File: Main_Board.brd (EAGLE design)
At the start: 160 x 100 mm, 73 parts, among them U1 RN4020RN4020, U2 LMS8117, U3 5V_BUCK_REG, Y1 MC-30632.768K-E3, Y2 MA-5066-25.0000M-C0

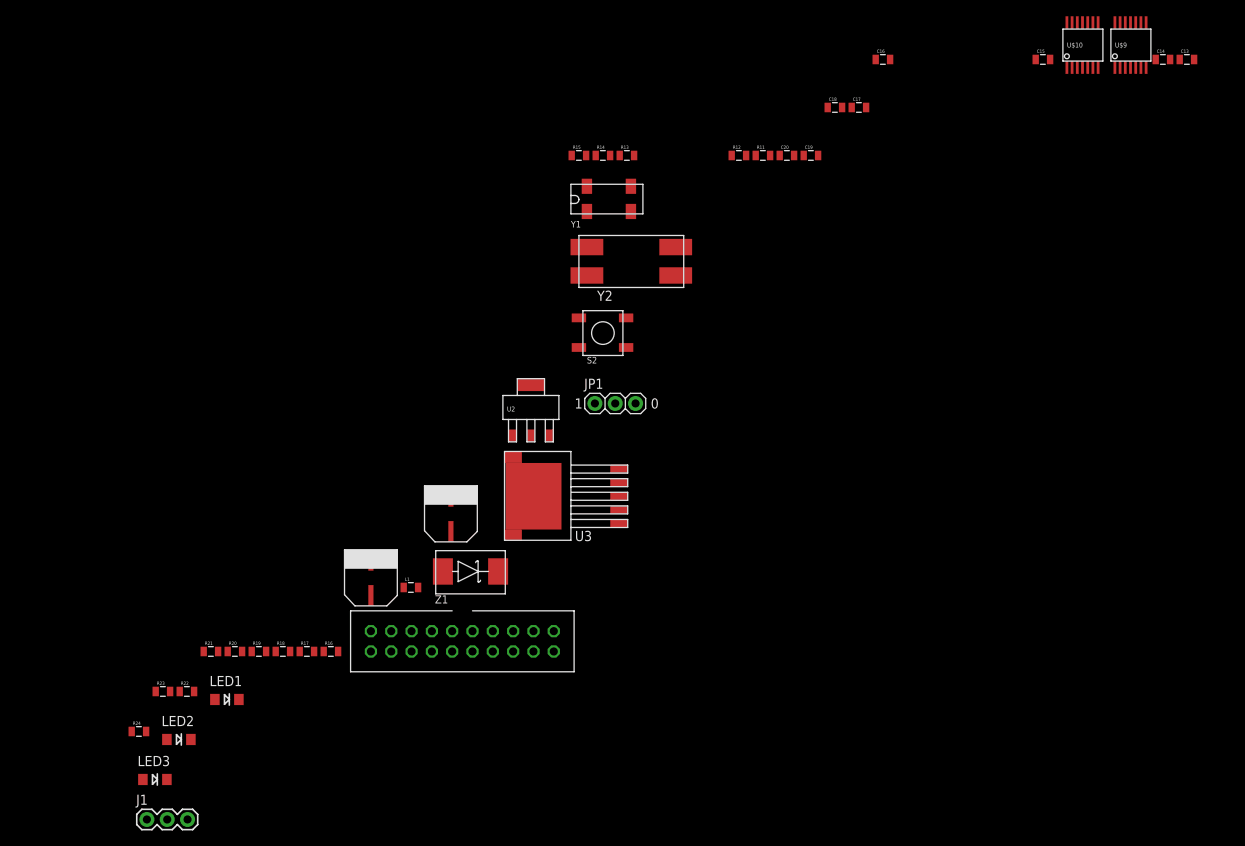
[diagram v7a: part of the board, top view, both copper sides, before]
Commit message: Added cap values
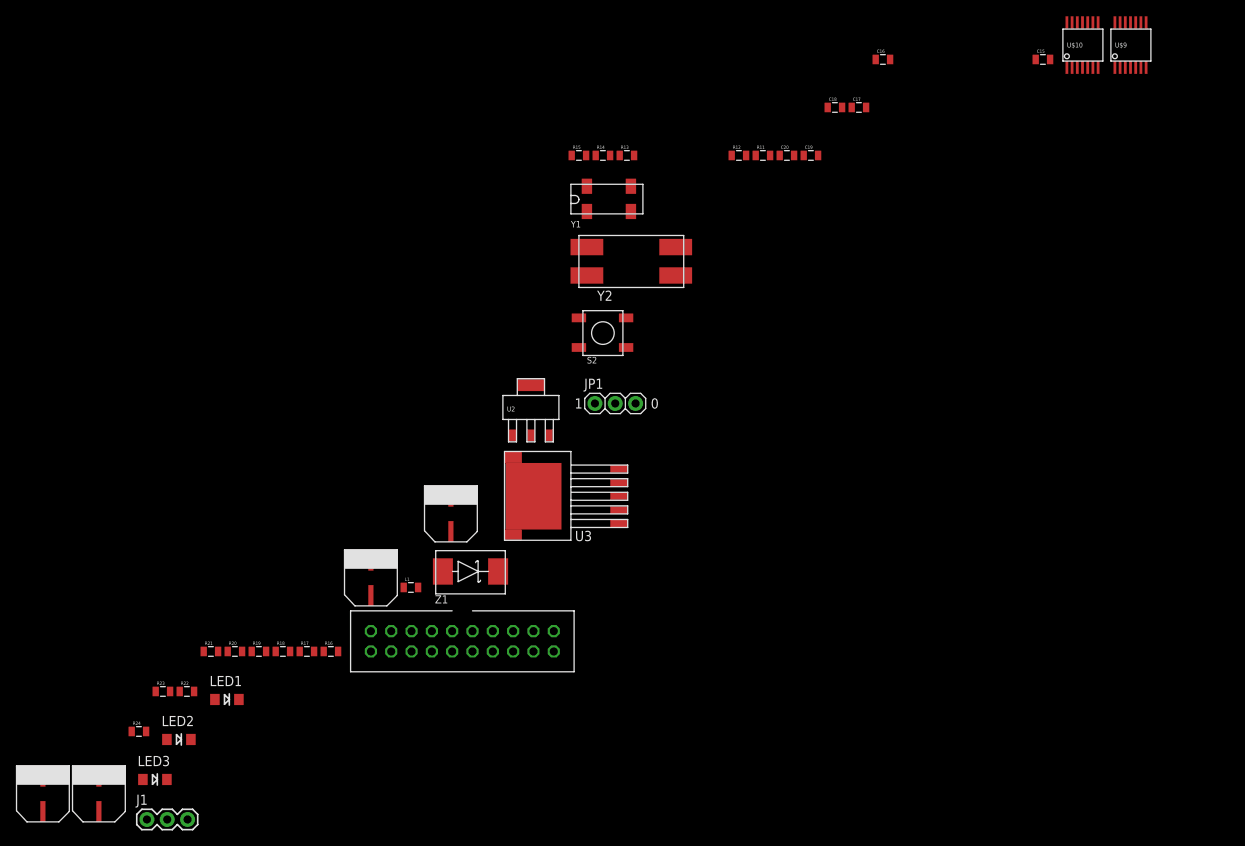
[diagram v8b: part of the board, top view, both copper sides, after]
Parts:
- removed C13, C14: (no value), SparkFun-Capacitors:0805
- added U$13, U$14: 10uF, BB8:RADIAL_CAN_SMD
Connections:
- net 3.3V: now also U$14.P$1; no longer C14.1
- net 5V: now also U$13.P$1; no longer C13.1
- net GND: now also U$13.P$2, U$14.P$2; no longer C13.2, C14.2
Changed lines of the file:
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@@
 <element name="FRAME1" library="SparkFun-Aesthetics" package="CREATIVE_COMMONS" value="FRAME-LEDGER" x="-87" y="-123"/>
 <element name="FRAME3" library="SparkFun-Aesthetics" package="CREATIVE_COMMONS" value="FRAME-LEDGER" x="-87" y="-132"/>
-<element name="C13" library="SparkFun-Capacitors" package="0805" value="" x="-118" y="-131"/>
-<element name="C14" library="SparkFun-Capacitors" package="0805" value="" x="-121" y="-131"/>
 <element name="U$9" library="BB8" package="14-TSSOP" value="SN74LV4T125" x="-127" y="-132"/>
 <element name="U$10" library="BB8" package="14-TSSOP" value="SN74LV4T125" x="-133" y="-132"/>
@@
 <element name="LED3" library="LilyPad-Wearables" package="LED-1206" value="" x="-247" y="-221"/>
 <element name="J1" library="SparkFun-Connectors" package="1X03" value="" x="-248" y="-226"/>
+<element name="U$13" library="BB8" package="RADIAL_CAN_SMD" value="10uF" x="-254" y="-225"/>
+<element name="U$14" library="BB8" package="RADIAL_CAN_SMD" value="10uF" x="-261" y="-225"/>
 </elements>
 <signals>
@@
 <contactref element="C12" pad="2"/>
 <contactref element="C11" pad="2"/>
-<contactref element="C13" pad="2"/>
-<contactref element="C14" pad="2"/>
 <contactref element="U$9" pad="P$1"/>
 <contactref element="U$9" pad="P$4"/>
@@
 <contactref element="LED3" pad="C"/>
 <contactref element="U$10" pad="P$10"/>
+<contactref element="U$13" pad="P$2"/>
+<contactref element="U$14" pad="P$2"/>
 <wire x1="-125.05" y1="-132" x2="-123.1" y2="-132" width="0" layer="19" extent="1-1"/>
 <wire x1="-127" y1="-132" x2="-125.05" y2="-132" width="0" layer="19" extent="1-1"/>
@@
 <wire x1="-131.05" y1="-132" x2="-129.1" y2="-132" width="0" layer="19" extent="1-1"/>
 <wire x1="-133" y1="-132" x2="-131.05" y2="-132" width="0" layer="19" extent="1-1"/>
-<wire x1="-120.1" y1="-131" x2="-123.1" y2="-132" width="0" layer="19" extent="1-1"/>
-<wire x1="-117.1" y1="-131" x2="-120.1" y2="-131" width="0" layer="19" extent="1-1"/>
 <wire x1="-136.9" y1="-131" x2="-133" y2="-132" width="0" layer="19" extent="1-1"/>
 <wire x1="-126.35" y1="-126.4" x2="-127" y2="-132" width="0" layer="19" extent="1-1"/>
@@
 <wire x1="-242.5" y1="-216" x2="-236.5" y2="-211" width="0" layer="19" extent="1-1"/>
 <wire x1="-245.5" y1="-221" x2="-242.5" y2="-216" width="0" layer="19" extent="1-1"/>
+<wire x1="-254" y1="-220.6" x2="-245.5" y2="-221" width="0" layer="19" extent="1-1"/>
+<wire x1="-261" y1="-220.6" x2="-254" y2="-220.6" width="0" layer="19" extent="1-1"/>
 <wire x1="-106.1" y1="-95" x2="-124.4" y2="-126.4" width="0" layer="19" extent="1-1"/>
 <wire x1="-103.1" y1="-95" x2="-106.1" y2="-95" width="0" layer="19" extent="1-1"/>
@@
 <contactref element="U$3" pad="VCC"/>
 <contactref element="U$4" pad="VCC"/>
-<contactref element="C13" pad="1"/>
 <contactref element="U$10" pad="P$14"/>
 <contactref element="U$10" pad="P$13"/>
 <contactref element="U2" pad="P$3"/>
-<wire x1="-132.35" y1="-126.4" x2="-118.9" y2="-131" width="0" layer="19" extent="1-1"/>
-<wire x1="-133" y1="-126.4" x2="-132.35" y2="-126.4" width="0" layer="19" extent="1-1"/>
-<wire x1="-197.7" y1="-178" x2="-133" y2="-126.4" width="0" layer="19" extent="1-1"/>
-<wire x1="-40.64" y1="-35.56" x2="-118.9" y2="-131" width="0" layer="19" extent="1-1"/>
+<contactref element="U$13" pad="P$1"/>
+<wire x1="-197.7" y1="-178" x2="-254" y2="-225" width="0" layer="19" extent="1-1"/>
+<wire x1="-133" y1="-126.4" x2="-197.7" y2="-178" width="0" layer="19" extent="1-1"/>
+<wire x1="-132.35" y1="-126.4" x2="-133" y2="-126.4" width="0" layer="19" extent="1-1"/>
+<wire x1="-40.64" y1="-35.56" x2="-132.35" y2="-126.4" width="0" layer="19" extent="1-1"/>
 <wire x1="-15.24" y1="-13.97" x2="-40.64" y2="-35.56" width="0" layer="19" extent="1-1"/>
 </signal>
@@
 <contactref element="C10" pad="2"/>
 <contactref element="C9" pad="2"/>
-<contactref element="C14" pad="1"/>
 <contactref element="U$9" pad="P$14"/>
 <contactref element="U1" pad="P$23"/>
@@
 <contactref element="U$12" pad="P$1"/>
 <contactref element="U$12" pad="P$2"/>
-<wire x1="-121.9" y1="-131" x2="-127" y2="-126.4" width="0" layer="19" extent="1-1"/>
+<contactref element="U$14" pad="P$1"/>
 <wire x1="-135.1" y1="-131" x2="-127" y2="-126.4" width="0" layer="19" extent="1-1"/>
 <wire x1="-100.1" y1="-95" x2="-127" y2="-126.4" width="0" layer="19" extent="1-1"/>
@@
 <wire x1="-197.14" y1="-202.46" x2="-200" y2="-178" width="0" layer="19" extent="1-1"/>
 <wire x1="-197.14" y1="-205" x2="-197.14" y2="-202.46" width="0" layer="19" extent="1-1"/>
+<wire x1="-261" y1="-225" x2="-197.14" y2="-205" width="0" layer="19" extent="1-1"/>
 </signal>
 <signal name="N$15">
